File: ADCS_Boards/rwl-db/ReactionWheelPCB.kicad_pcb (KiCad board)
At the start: 4 copper layers, 90.2 x 95.9 mm, 37 parts, among them J1 PC104_Connector, J2 Conn_1, J3 Conn_2, J4 Conn_3, J5 Conn_4, U1 Controller 1, U2 Controller 2, U3 Controller 3, U4 Controller 4, U5 LM358, U6 LM358

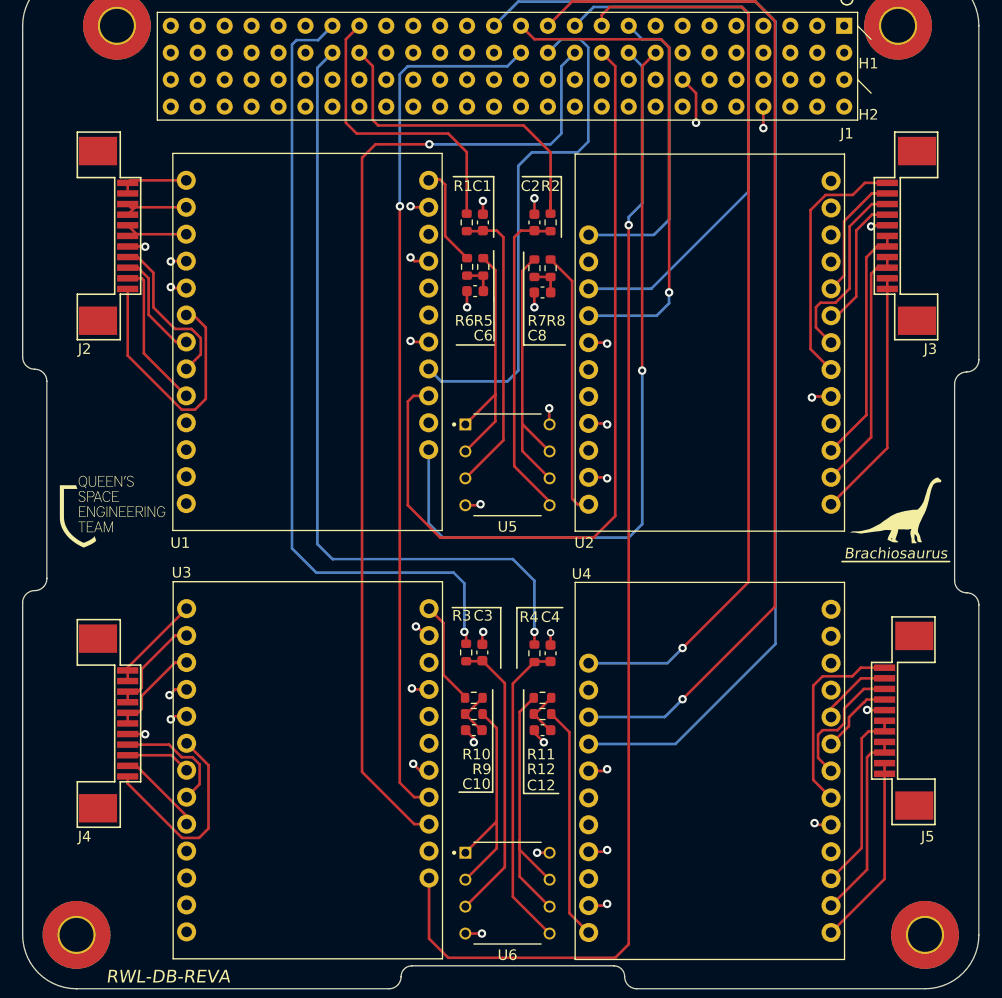
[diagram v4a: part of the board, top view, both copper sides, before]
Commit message: adcs: rwl-db: include new vertical connectors and step models
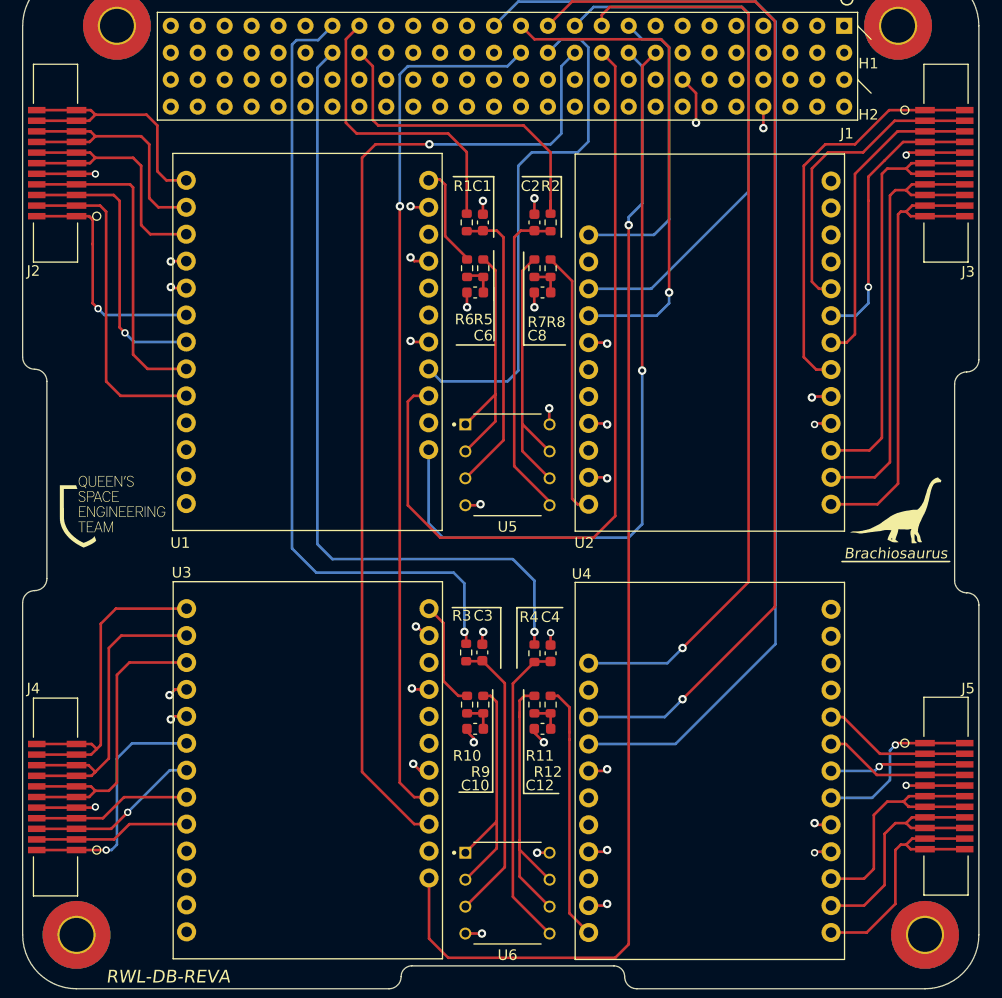
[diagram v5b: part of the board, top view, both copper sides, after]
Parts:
- J2: value Conn_1 -> Conn_02x11_Odd_Even; footprint qset-footprints:FPC_11_SAT_1-84953-1 -> qset-footprints:1-1734248-1-reaction-wheel-connector
- J3: value Conn_2 -> Conn_02x11_Odd_Even; footprint qset-footprints:FPC_11_SAT_1-84953-1 -> qset-footprints:1-1734248-1-reaction-wheel-connector
- J4: value Conn_3 -> Conn_02x11_Odd_Even; footprint qset-footprints:FPC_11_SAT_1-84953-1 -> qset-footprints:1-1734248-1-reaction-wheel-connector
- J5: value Conn_4 -> Conn_02x11_Odd_Even; footprint qset-footprints:FPC_11_SAT_1-84953-1 -> qset-footprints:1-1734248-1-reaction-wheel-connector
- R10, R12, R6, R8: value 10k -> 1M
- R11, R5, R7, R9: value 10k -> 5k
- moved J4 12.9 mm to (114.3, 129.8)
- moved J3 12.4 mm to (194.3, 60.0)
- moved J2 5.17 mm to (114.3, 70.0)
- moved J5 4.35 mm to (194.3, 119.7)
- moved R9 1.26 mm to (152.7, 116.1), turned to 90 degrees
- moved R12 1.17 mm to (159.0, 116.1), turned to 90 degrees
- moved R11 0.99 mm to (157.5, 116.1), turned to -90 degrees
- moved R10 0.90 mm to (151.1, 116.1), turned to -90 degrees
- moved C10 0.18 mm to (151.9, 118.4)
- moved R5 0.13 mm to (152.7, 74.9)
- moved R6 0.13 mm to (151.1, 74.9)
- moved C12 0.13 mm to (158.2, 118.4)
- moved C6 0.13 mm to (151.9, 77.2)
- turned R8 to 90 degrees
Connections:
- J2 pad 10: Net-(U1-Pad1) -> GND
- J2 pad 11: Net-(U1-Pad1) -> Net-(U1-Pad3)
- J2 pad 2: Net-(U1-Pad9) -> Net-(U1-Pad6)
- J2 pad 3: Net-(U1-Pad7) -> Net-(U1-Pad9)
- J2 pad 4: Net-(U1-Pad8) -> Net-(U1-Pad9)
- J2 pad 5: GND -> Net-(U1-Pad7)
- J2 pad 6: Net-(U1-Pad3) -> Net-(U1-Pad7)
- J2 pad 7: Net-(U1-Pad3) -> Net-(U1-Pad8)
- J2 pad 8: Net-(U1-Pad2) -> Net-(U1-Pad8)
- J2 pad 9: Net-(U1-Pad2) -> GND
- J3 pad 10: Net-(U2-Pad1) -> GND
- J3 pad 11: Net-(U2-Pad1) -> Net-(U2-Pad3)
- J3 pad 2: Net-(U2-Pad9) -> Net-(U2-Pad6)
- J3 pad 3: Net-(U2-Pad7) -> Net-(U2-Pad9)
- J3 pad 4: Net-(U2-Pad8) -> Net-(U2-Pad9)
- J3 pad 5: GND -> Net-(U2-Pad7)
- J3 pad 6: Net-(U2-Pad3) -> Net-(U2-Pad7)
- J3 pad 7: Net-(U2-Pad3) -> Net-(U2-Pad8)
- J3 pad 8: Net-(U2-Pad2) -> Net-(U2-Pad8)
- J3 pad 9: Net-(U2-Pad2) -> GND
- J4 pad 10: Net-(U3-Pad1) -> GND
- J4 pad 11: Net-(U3-Pad1) -> Net-(U3-Pad3)
- J4 pad 2: Net-(U3-Pad9) -> Net-(U3-Pad6)
- J4 pad 3: Net-(U3-Pad7) -> Net-(U3-Pad9)
- J4 pad 4: Net-(U3-Pad8) -> Net-(U3-Pad9)
- J4 pad 5: GND -> Net-(U3-Pad7)
- J4 pad 6: Net-(U3-Pad3) -> Net-(U3-Pad7)
- J4 pad 7: Net-(U3-Pad3) -> Net-(U3-Pad8)
- J4 pad 8: Net-(U3-Pad2) -> Net-(U3-Pad8)
- J4 pad 9: Net-(U3-Pad2) -> GND
- J5 pad 10: Net-(U4-Pad1) -> GND
- J5 pad 11: Net-(U4-Pad1) -> Net-(U4-Pad3)
- J5 pad 2: Net-(U4-Pad9) -> Net-(U4-Pad6)
- J5 pad 3: Net-(U4-Pad7) -> Net-(U4-Pad9)
- J5 pad 4: Net-(U4-Pad8) -> Net-(U4-Pad9)
- J5 pad 5: GND -> Net-(U4-Pad7)
- J5 pad 6: Net-(U4-Pad3) -> Net-(U4-Pad7)
- J5 pad 7: Net-(U4-Pad3) -> Net-(U4-Pad8)
- J5 pad 8: Net-(U4-Pad2) -> Net-(U4-Pad8)
- J5 pad 9: Net-(U4-Pad2) -> GND
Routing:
- net Net-(U3-Pad1): track 9.13 -> 32.4 mm
- net Net-(U3-Pad3): track 9.24 -> 31.0 mm
- net Net-(U3-Pad2): track 9.78 -> 31.5 mm
- net Net-(U2-Pad1): track 23.5 -> 44.9 mm
- net Net-(U2-Pad3): track 23.0 -> 44.1 mm
- net Net-(U2-Pad2): track 23.5 -> 44.5 mm
- net Net-(U1-Pad3): track 5.87 -> 26.3 mm
- net Net-(U1-Pad2): track 6.64 -> 25.8 mm
- net Net-(U1-Pad1): track 6.62 -> 25.1 mm
- net Net-(U2-Pad9): track 12.0 -> 29.0 mm
- net Net-(U1-Pad9): track 14.1 -> 30.9 mm
- net Net-(U1-Pad7): track 10.4 -> 26.8 mm, vias 0 -> 1
- net GND: track 48.1 -> 63.8 mm
- net Net-(U1-Pad8): track 15.4 -> 30.5 mm
- net Net-(U2-Pad6): track 24.1 -> 38.4 mm
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
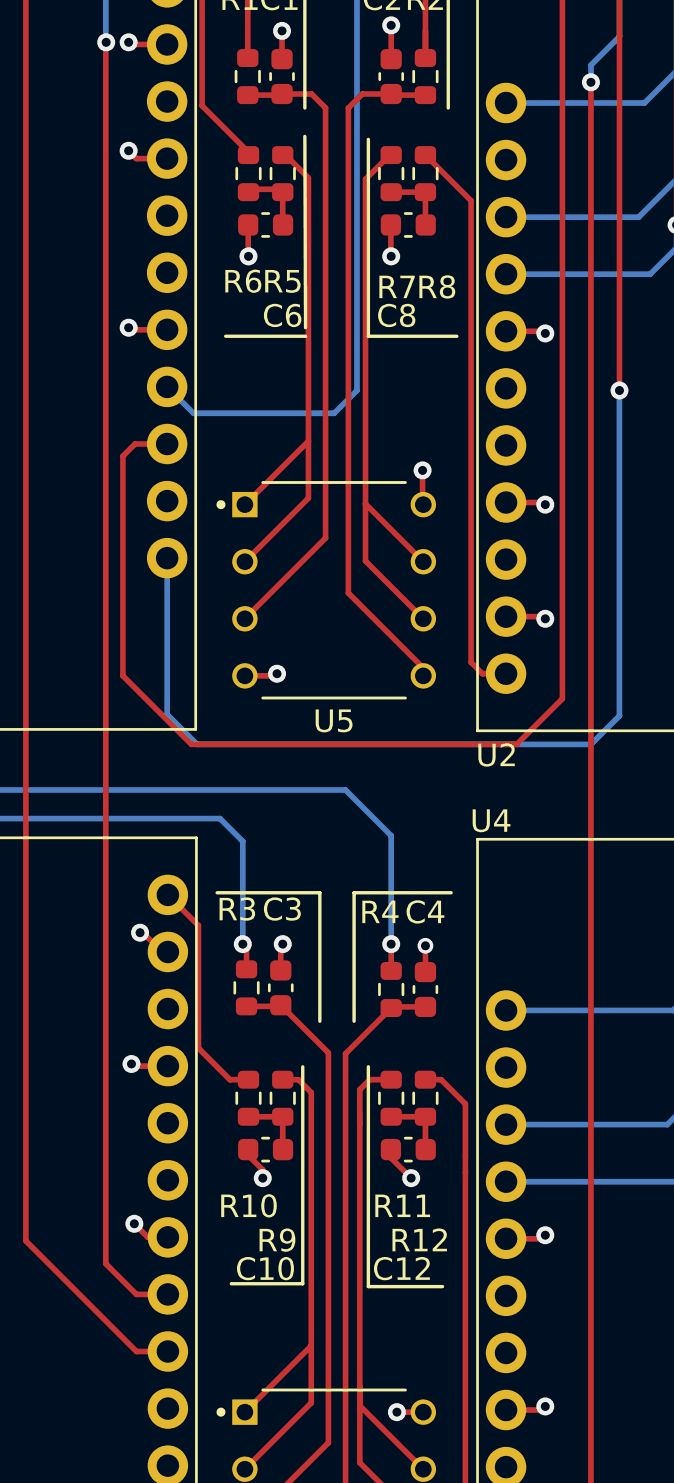
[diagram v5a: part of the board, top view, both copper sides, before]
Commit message: adcs: rwl-db: updated 5k resistors to use 0402
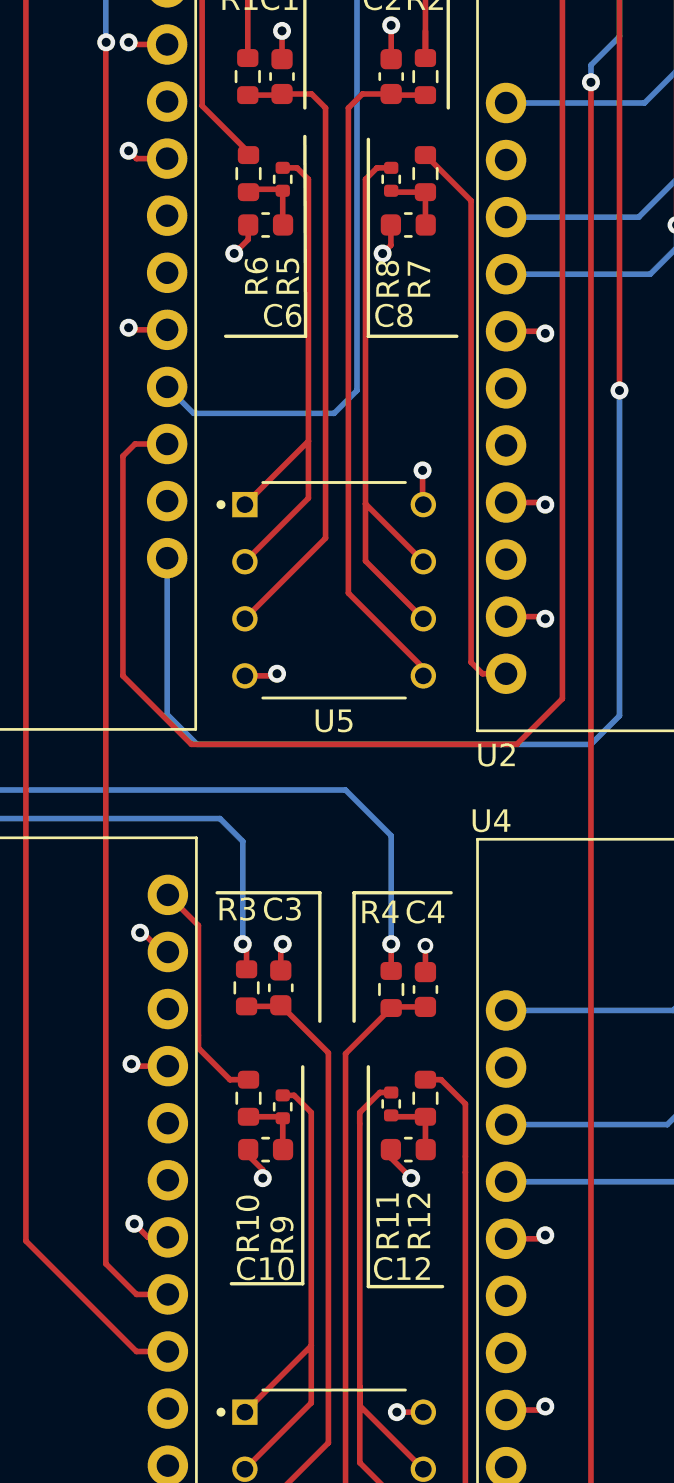
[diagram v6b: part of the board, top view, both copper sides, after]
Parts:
- R11, R5, R7, R9: footprint Resistor_SMD:R_0603_1608Metric -> Resistor_SMD:R_0402_1005Metric
- moved R9 0.38 mm to (152.7, 116.5)
- moved R11 0.25 mm to (157.5, 116.3)
- moved R5 0.25 mm to (152.7, 75.2)
- moved R7 0.25 mm to (157.5, 75.2)
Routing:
- net Net-(R11-Pad1): track 27.5 -> 26.2 mm
- net Net-(R9-Pad2): track 23.7 -> 22.9 mm

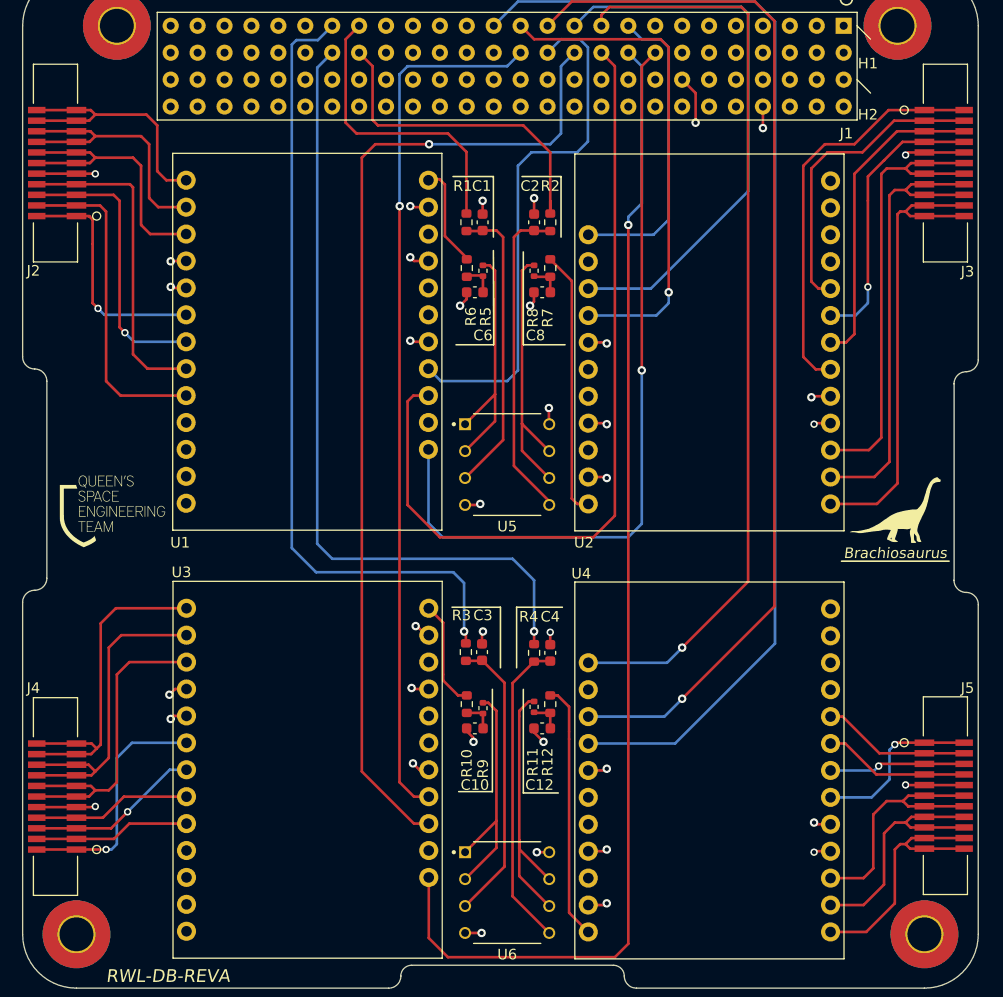
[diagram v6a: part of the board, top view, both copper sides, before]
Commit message: adcs: rwl-db: move connectors to left and right centre of PCB
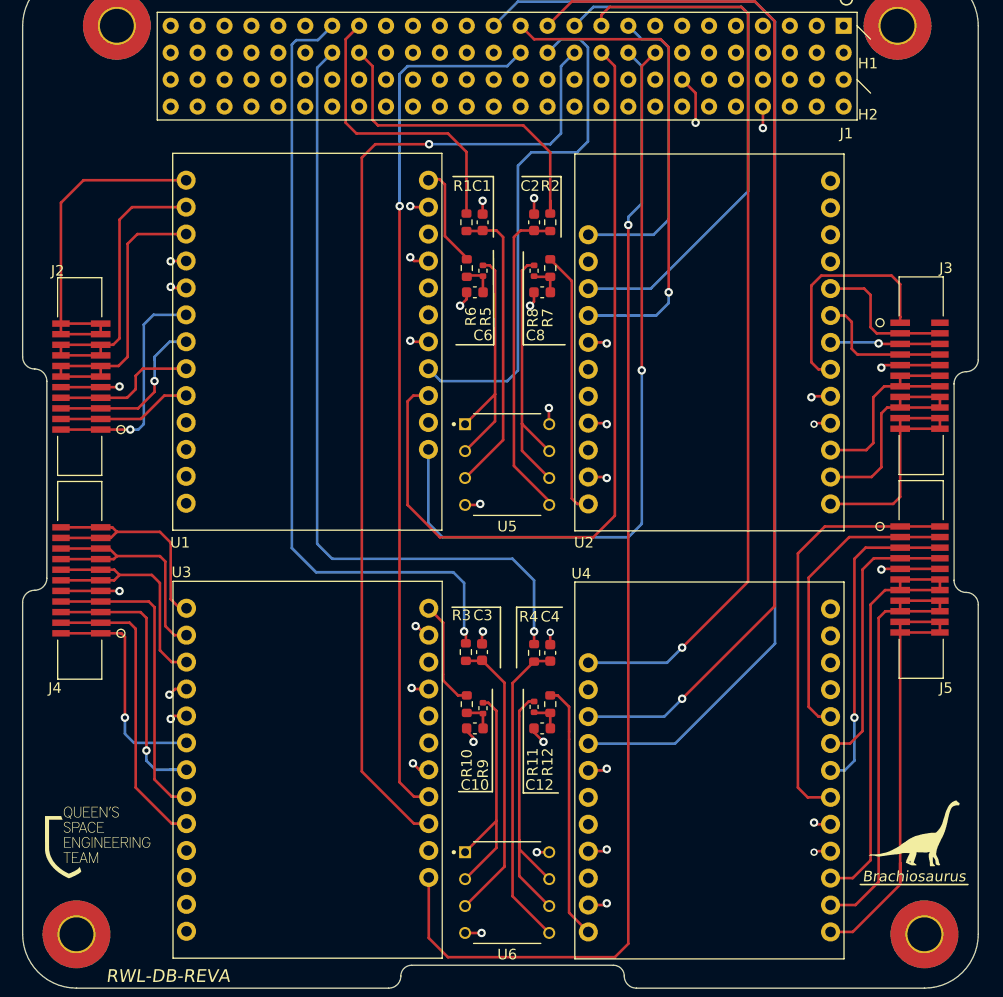
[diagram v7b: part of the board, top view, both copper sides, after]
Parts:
- moved G*** 31.3 mm to (116.3, 129.0)
- moved Brachiosaurus 30.6 mm to (194.1, 128.3)
- moved J4 20.5 mm to (116.6, 109.4)
- moved J5 20.5 mm to (192.0, 99.3)
- moved J2 20.3 mm to (116.6, 90.2)
- moved J3 20.2 mm to (192.0, 80.1)
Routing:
- net Net-(U2-Pad3): track 44.1 -> 20.1 mm
- net Net-(U4-Pad6): track 16.4 -> 40.0 mm, vias 1 -> 0
- net Net-(U2-Pad2): track 44.5 -> 21.8 mm
- net Net-(U2-Pad1): track 44.9 -> 22.8 mm
- net Net-(U2-Pad7): track 29.7 -> 10.4 mm, vias 0 -> 1
- net Net-(U4-Pad1): track 25.0 -> 43.5 mm
- net Net-(U1-Pad9): track 30.9 -> 12.7 mm
- net Net-(U4-Pad2): track 24.6 -> 42.1 mm
- net Net-(U4-Pad7): track 12.9 -> 30.2 mm
- net Net-(U1-Pad8): track 30.5 -> 13.7 mm
- net Net-(U4-Pad3): track 24.8 -> 41.5 mm
- net Net-(U2-Pad6): track 38.4 -> 22.1 mm
- net Net-(U2-Pad9): track 29.0 -> 13.9 mm
- net Net-(U4-Pad9): track 14.0 -> 28.6 mm
- net Net-(U3-Pad8): track 15.0 -> 29.0 mm
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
